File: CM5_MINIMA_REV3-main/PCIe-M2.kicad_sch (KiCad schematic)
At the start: 22 parts, among them J701 Bus_M.2_Socket_M, M701 M.2 Solder Nut, M702 M.2 Solder Nut, M705 M.2 Screw, U702 AP3441SHE-7B, U703 ASEK-32.768KHZ-L-R-T

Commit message: warning fix - 0  in schematic
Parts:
- M701, M702: footprint _pico:MountingHole_3mm_Pad -> CM5_MINIMA_local:MountingHole_3mm_Pad
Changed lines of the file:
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@@
 			)
 		)
-		(property "Footprint" "_pico:MountingHole_3mm_Pad"
+		(property "Footprint" "CM5_MINIMA_local:MountingHole_3mm_Pad"
 			(at 251.46 87.63 0)
 			(effects
@@
 			)
 		)
-		(property "Footprint" "_pico:MountingHole_3mm_Pad"
+		(property "Footprint" "CM5_MINIMA_local:MountingHole_3mm_Pad"
 			(at 251.46 104.14 0)
 			(effects

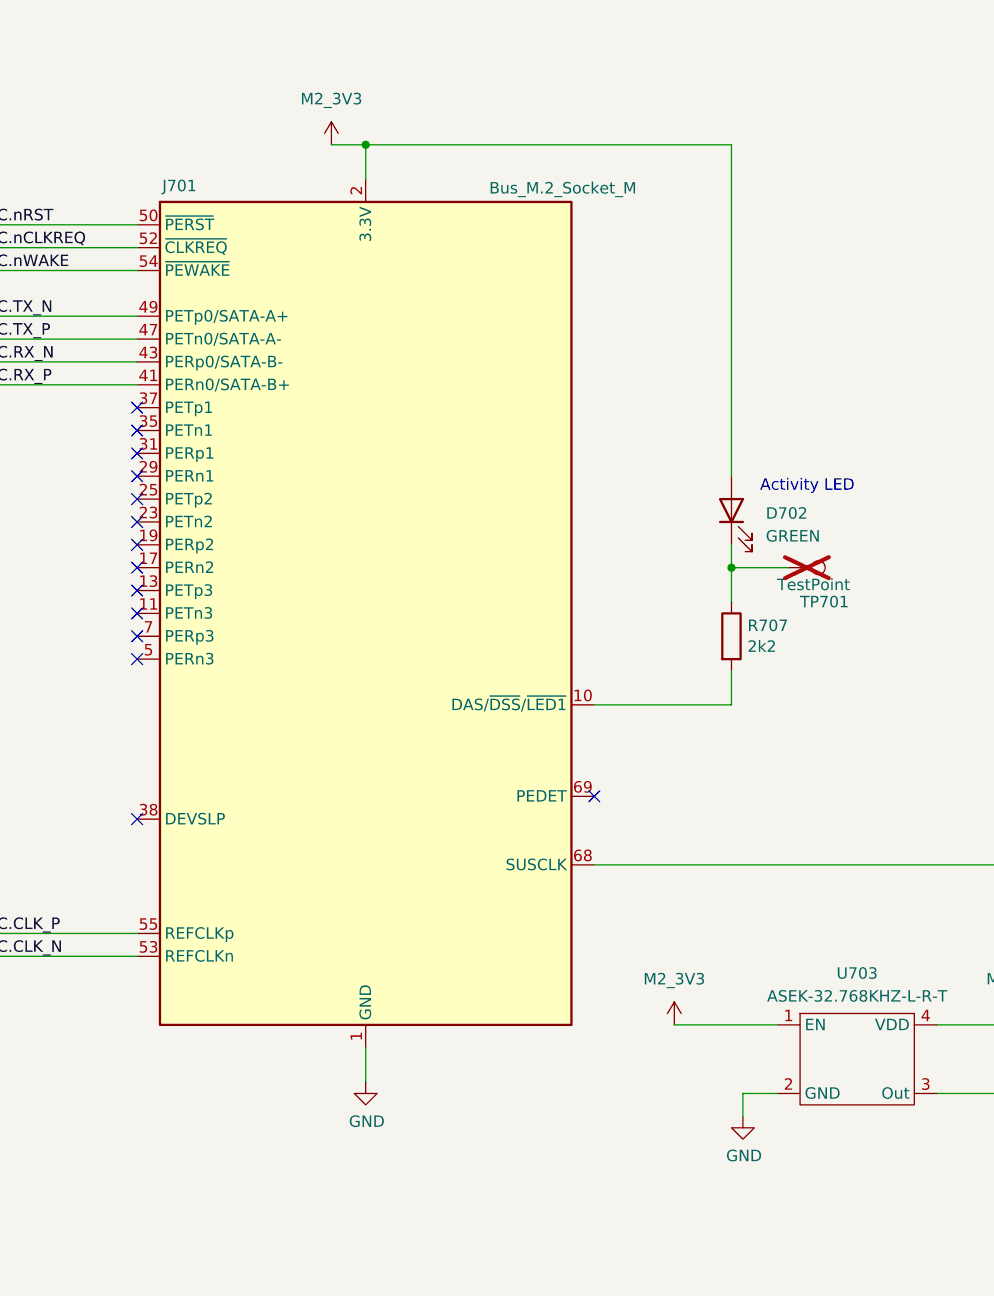
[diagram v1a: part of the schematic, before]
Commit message: Revert CM5_MINIMA_REV3-main to pre-warning-fix state (feae2c2) - fix component mismatches
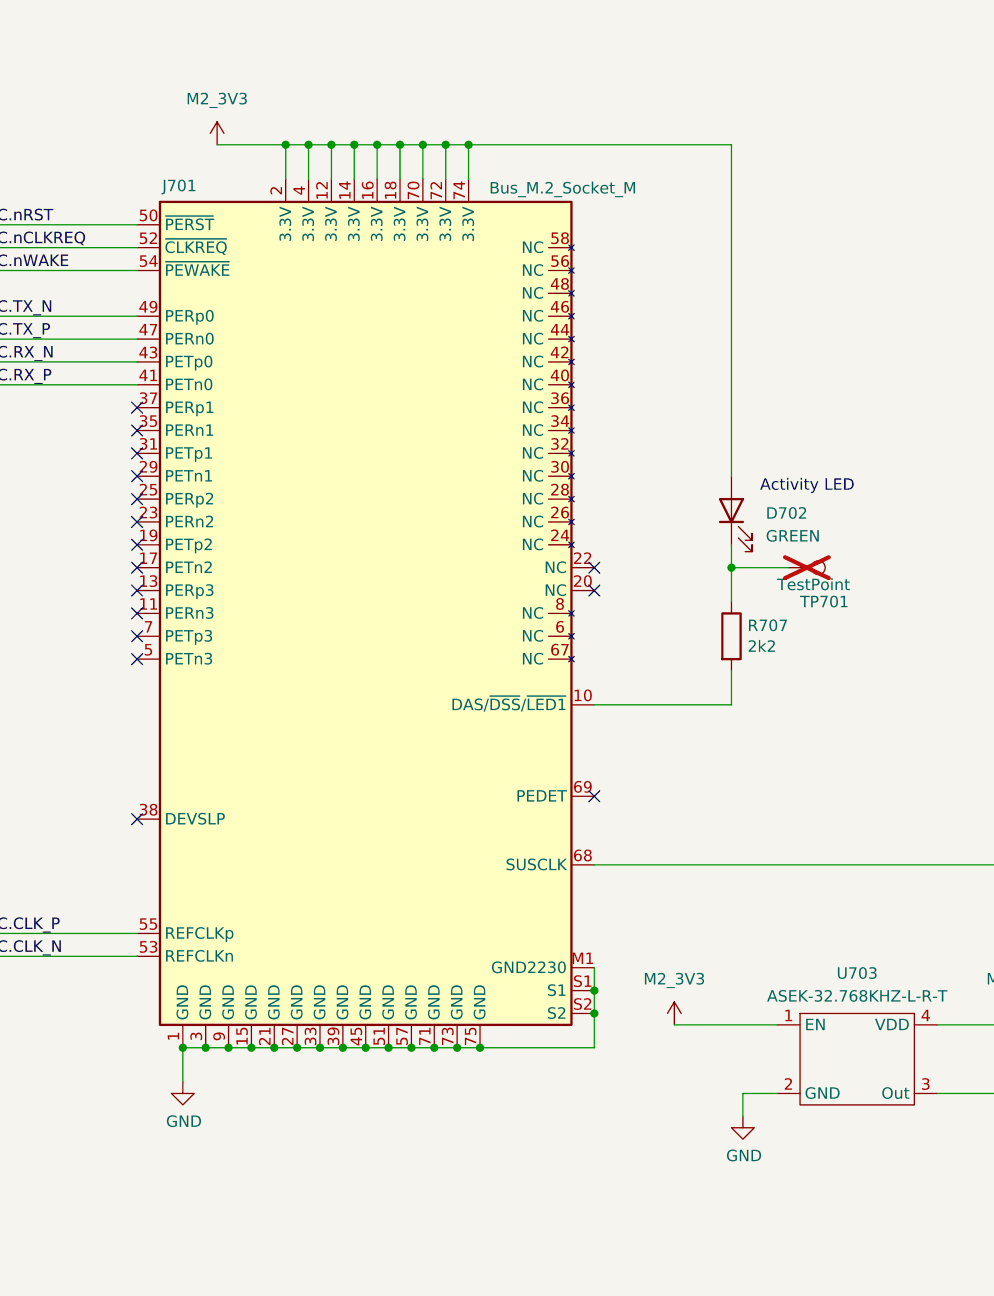
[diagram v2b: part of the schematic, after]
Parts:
- D702: footprint CM5_MINIMA_local:LED-SMD_L1.7-W0.6-RD -> EasyEDA:LED-SMD_L1.7-W0.6-RD
- J701: footprint CM5_MINIMA_local:M.2 M Key socket_2230_2242 -> CM5IO:M.2 M Key socket_2230_2242; symbol Connector_Bus_M.2_Socket_M:Bus_M.2_Socket_M -> CM5IO:Bus_M.2_Socket_M
- M701, M702: footprint CM5_MINIMA_local:MountingHole_3mm_Pad -> _pico:MountingHole_3mm_Pad
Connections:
- net GND: now also J701.M1 (GND2230), J701.S1, J701.S2
- no-connect marks 15 -> 17

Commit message: warning fix - 17 left
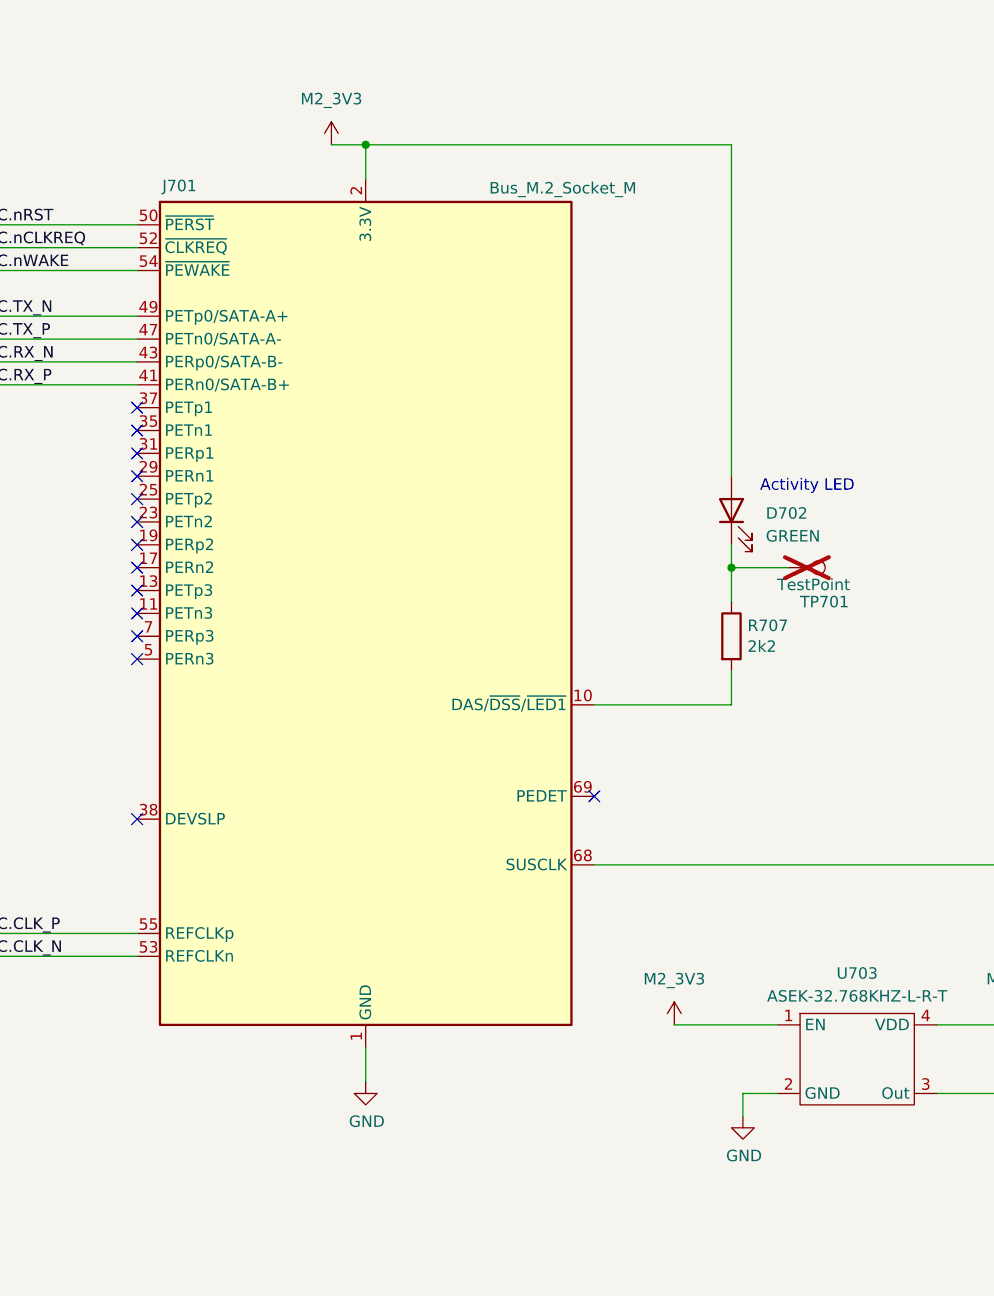
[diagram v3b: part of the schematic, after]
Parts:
- D702: footprint EasyEDA:LED-SMD_L1.7-W0.6-RD -> CM5_MINIMA_local:LED-SMD_L1.7-W0.6-RD
- J701: footprint CM5IO:M.2 M Key socket_2230_2242 -> CM5_MINIMA_local:M.2 M Key socket_2230_2242; symbol CM5IO:Bus_M.2_Socket_M -> Connector_Bus_M.2_Socket_M:Bus_M.2_Socket_M
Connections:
- net GND: no longer J701.M1 (GND2230), J701.S1, J701.S2
- no-connect marks 17 -> 15
